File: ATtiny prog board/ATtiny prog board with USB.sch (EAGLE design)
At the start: 11 parts, among them J1 CON_HEADER_1X06-PTH

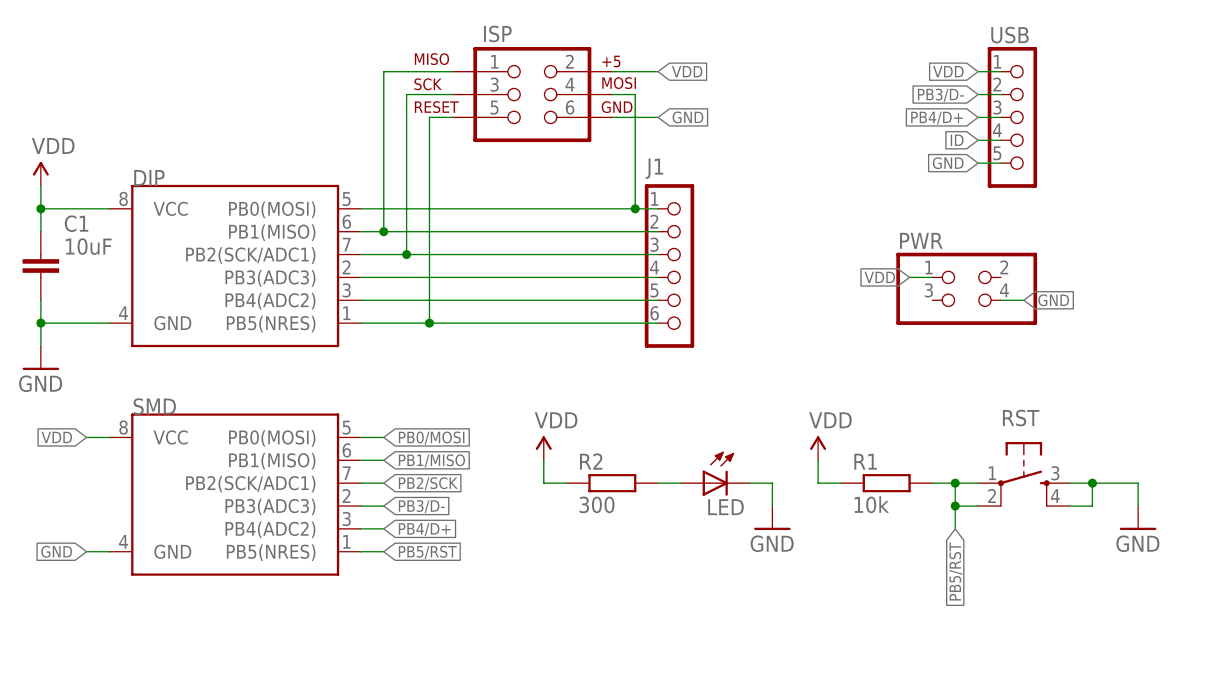
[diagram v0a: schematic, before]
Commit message: updated ATtiny prog board with USB
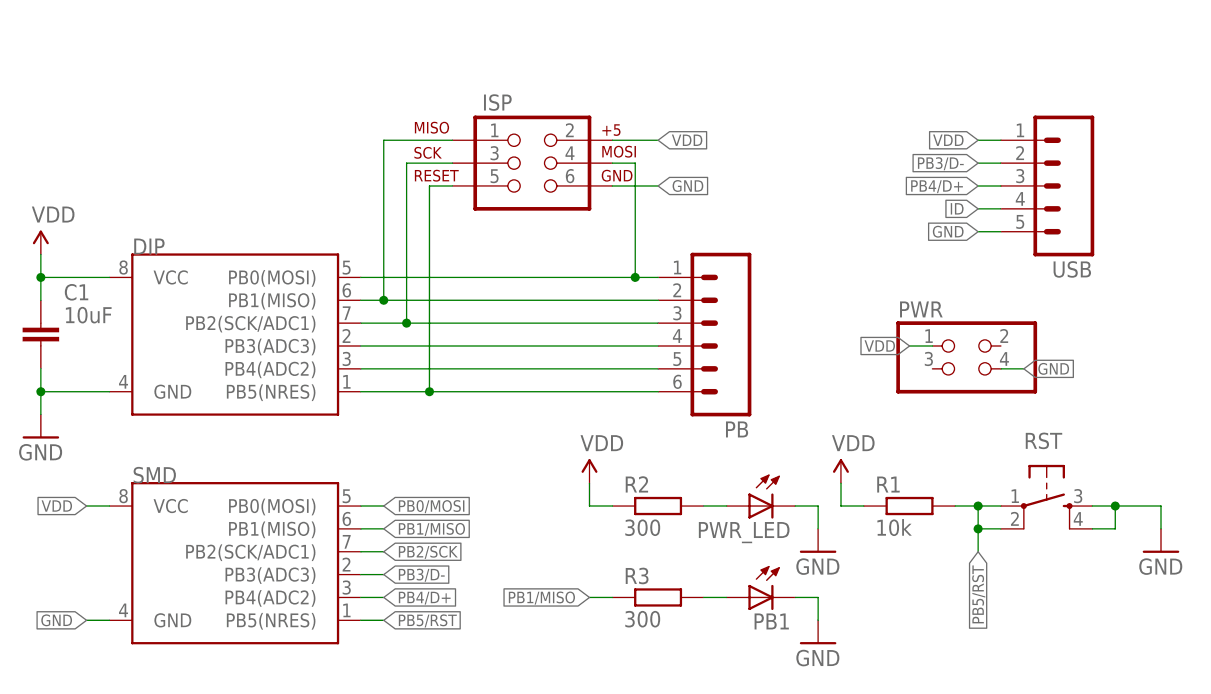
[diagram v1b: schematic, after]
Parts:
- removed J1: CON_HEADER_1X06-PTH, dp_devices:CON_HEADER_1X06-PTH
- removed LED: (no value), dp_devices:LED-0603
- added PB: (no value), SparkFun-Connectors:M06SILK_FEMALE_PTH
- added PB1, PWR_LED: (no value), dp_devices:LED-0805
- added R3: 300, dp_devices:RESISTOR-0603
- USB: value CON_HEADER_1X05-PTH -> (none); device dp_devices:CON_HEADER_1X05-PTH -> SparkFun-Connectors:M05PTH
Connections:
- new net N$2: PB1.A, R3.2
- net GND: now also PB1.C, PWR_LED.C; no longer LED.C
- net N$1: now also PWR_LED.A; no longer LED.A
- net PB0/MOSI: now also PB.1; no longer J1.1
- net PB1/MISO: now also PB.2, R3.1; no longer J1.2
- net PB2/SCK: now also PB.3; no longer J1.3
- net PB3/D-: now also PB.4; no longer J1.4
- net PB4/D+: now also PB.5; no longer J1.5
- net PB5/RST: now also PB.6; no longer J1.6
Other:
- moved on the sheet: C1, DIP, ISP, PWR, R1, R2, RST, SMD, USB
